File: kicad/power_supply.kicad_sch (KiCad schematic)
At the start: 16 parts, among them J5 Conn_01x02, U5 ISL85410FRZ-T7A

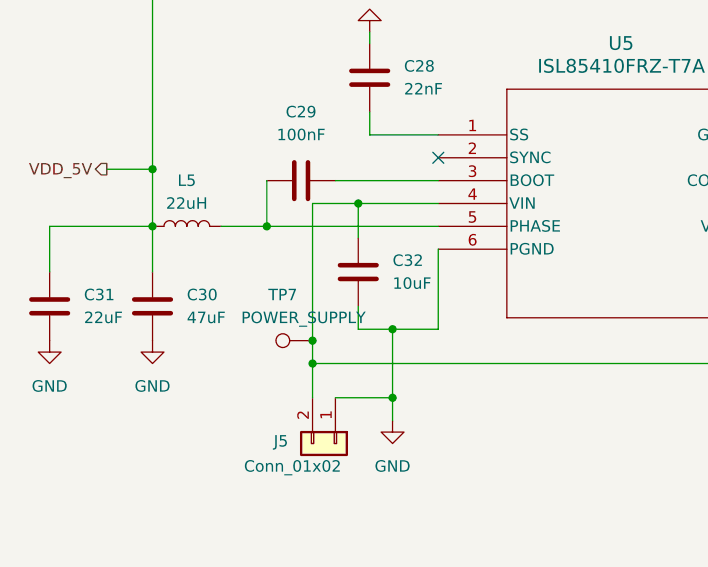
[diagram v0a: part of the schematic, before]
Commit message: feat: move TC2030
Signed-off-by: Bobo Bäck Engström <bobo@id8-engineering.io>
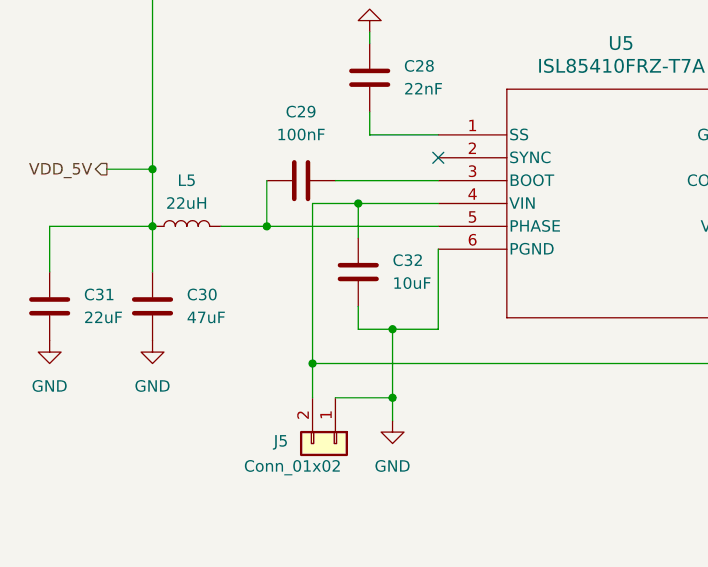
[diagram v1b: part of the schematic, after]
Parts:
- removed TP7: POWER_SUPPLY, seven-lib:TestPoint_Pad_2.0x2.0mm, symbol seven_lib:TestPoint
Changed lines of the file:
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@@
-	)
-	(junction
-		(at 53.34 102.87)
-		(diameter 0)
-		(color 0 0 0 0)
 	)
 	(junction
@@
 	(wire
 		(pts
-			(xy 53.34 87.63) (xy 53.34 102.87)
+			(xy 53.34 87.63) (xy 53.34 105.41)
 		)
 		(stroke
@@
 		(pts
 			(xy 53.34 105.41) (xy 107.95 105.41)
-		)
-		(stroke
-			(width 0)
-			(type default)
-		)
-	)
-	(wire
-		(pts
-			(xy 53.34 102.87) (xy 53.34 105.41)
 		)
 		(stroke
@@
 					(unit 1)
 				)
-			)
-		)
-	)
-	(symbol
-		(lib_id "seven_lib:TestPoint")
-		(at 53.34 102.87 90)
-		(unit 1)
-		(body_style 1)
-		(exclude_from_sim no)
-		(in_bom yes)
-		(on_board yes)
-		(in_pos_files yes)
-		(dnp no)
-		(property "Reference" "TP7"
-			(at 50.038 97.79 90)
-			(show_name no)
-			(do_not_autoplace no)
-			(effects
-				(font
-					(size 1.27 1.27)
-				)
-			)
-		)
-		(property "Value" "POWER_SUPPLY"
-			(at 52.324 100.33 90)
-			(show_name no)
-			(do_not_autoplace no)
-			(effects
-				(font
-					(size 1.27 1.27)
-				)
-			)
-		)
-		(property "Footprint" "seven-lib:TestPoint_Pad_2.0x2.0mm"
-			(at 53.34 97.79 0)
-			(hide yes)
-			(show_name no)
-			(do_not_autoplace no)
-			(effects
-				(font
-					(size 1.27 1.27)
-				)
-			)
-		)
-		(property "Datasheet" ""
-			(at 53.34 97.79 0)
-			(hide yes)
-			(show_name no)
-			(do_not_autoplace no)
-			(effects
-				(font
-					(size 1.27 1.27)
-				)
-			)
-		)
-		(property "Description" "test point"
-			(at 53.34 102.87 0)
-			(hide yes)
-			(show_name no)
-			(do_not_autoplace no)
-			(effects
-				(font
-					(size 1.27 1.27)
-				)
-			)
-		)
-		(property "Manufacturer Part Number" ""
-			(at 53.34 102.87 90)
-			(hide yes)
-			(show_name no)
-			(do_not_autoplace no)
-			(effects
-				(font
-					(size 1.27 1.27)
-				)
-			)
-		)
-		(pin "1"
-		)
-		(instances
-			(project "seven"
-				(path "/8e3cc843-5797-49f3-8b3a-1c11450ccd1e/212f259f-7773-4a20-96f5-c599a3d0b814"
-					(reference "TP7")
-					(unit 1)
-				)
